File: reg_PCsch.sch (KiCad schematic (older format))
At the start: 41 parts, among them U178 74LS03, U181 74HC244, U182 74HC244, U194 74HC244, U195 74HC244, U215 74HC193, U216 74HC193, U217 74HC193, U218 74HC193

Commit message: place leds and inverters for the iBn bus
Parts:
- B31, B32: value 22K -> 2.2K
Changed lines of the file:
@@
 P 3550 13750
 F 0 "B32" H 3071 13704 50  0000 R CNN
-F 1 "22K" H 3071 13795 50  0000 R CNN
+F 1 "2.2K" H 3071 13795 50  0000 R CNN
 F 2 "Resistor_THT:R_Array_SIP9" V 4025 13750 50  0001 C CNN
 F 3 "http://www.vishay.com/docs/31509/csc.pdf" H 3550 13750 50  0001 C CNN
@@
 P 6650 13750
 F 0 "B31" H 6170 13704 50  0000 R CNN
-F 1 "22K" H 6170 13795 50  0000 R CNN
+F 1 "2.2K" H 6170 13795 50  0000 R CNN
 F 2 "Resistor_THT:R_Array_SIP9" V 7125 13750 50  0001 C CNN
 F 3 "http://www.vishay.com/docs/31509/csc.pdf" H 6650 13750 50  0001 C CNN

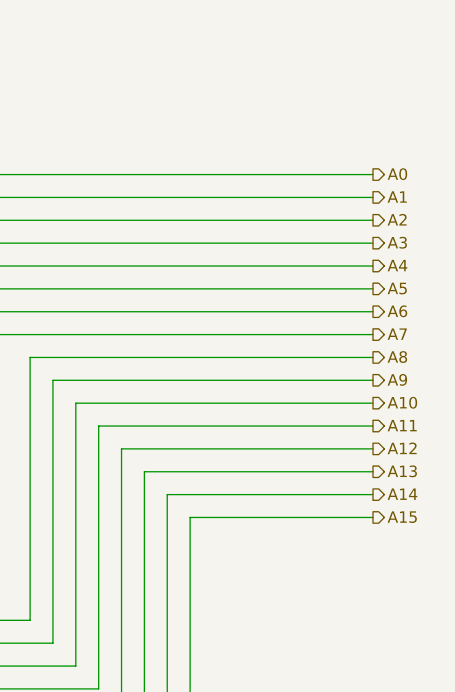
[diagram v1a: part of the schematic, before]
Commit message: oops, had to redo part of the PC because I inverted U182 and U195, also routed A0-A7 through the PC register
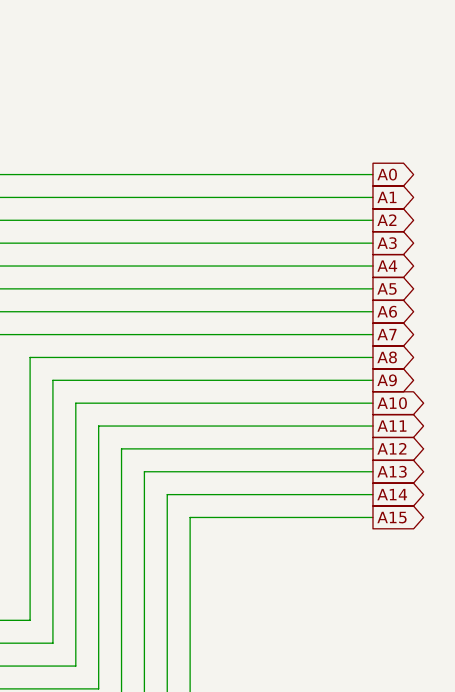
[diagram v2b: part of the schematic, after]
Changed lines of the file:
@@
 Wire Wire Line
 	7750 3350 10000 3350
-Text HLabel 10000 3350 2    50   Output ~ 0
-A0
-Text HLabel 10000 3450 2    50   Output ~ 0
-A1
-Text HLabel 10000 3550 2    50   Output ~ 0
-A2
-Text HLabel 10000 3650 2    50   Output ~ 0
-A3
-Text HLabel 10000 3750 2    50   Output ~ 0
-A4
-Text HLabel 10000 3850 2    50   Output ~ 0
-A5
-Text HLabel 10000 3950 2    50   Output ~ 0
-A6
-Text HLabel 10000 4050 2    50   Output ~ 0
-A7
-Text HLabel 10000 4150 2    50   Output ~ 0
-A8
-Text HLabel 10000 4250 2    50   Output ~ 0
-A9
-Text HLabel 10000 4350 2    50   Output ~ 0
-A10
-Text HLabel 10000 4450 2    50   Output ~ 0
-A11
-Text HLabel 10000 4550 2    50   Output ~ 0
-A12
-Text HLabel 10000 4650 2    50   Output ~ 0
-A13
-Text HLabel 10000 4750 2    50   Output ~ 0
-A14
-Text HLabel 10000 4850 2    50   Output ~ 0
-A15
 $Comp
 L power:VCC #PWR0198
@@
 Text GLabel 1000 7200 0    50   Input ~ 0
 PCHregWR
+Text GLabel 10000 3350 2    50   Output ~ 0
+A0
+Text GLabel 10000 3450 2    50   Output ~ 0
+A1
+Text GLabel 10000 3550 2    50   Output ~ 0
+A2
+Text GLabel 10000 3650 2    50   Output ~ 0
+A3
+Text GLabel 10000 3750 2    50   Output ~ 0
+A4
+Text GLabel 10000 3850 2    50   Output ~ 0
+A5
+Text GLabel 10000 3950 2    50   Output ~ 0
+A6
+Text GLabel 10000 4050 2    50   Output ~ 0
+A7
+Text GLabel 10000 4150 2    50   Output ~ 0
+A8
+Text GLabel 10000 4250 2    50   Output ~ 0
+A9
+Text GLabel 10000 4350 2    50   Output ~ 0
+A10
+Text GLabel 10000 4450 2    50   Output ~ 0
+A11
+Text GLabel 10000 4550 2    50   Output ~ 0
+A12
+Text GLabel 10000 4650 2    50   Output ~ 0
+A13
+Text GLabel 10000 4750 2    50   Output ~ 0
+A14
+Text GLabel 10000 4850 2    50   Output ~ 0
+A15
 $EndSCHEMATC

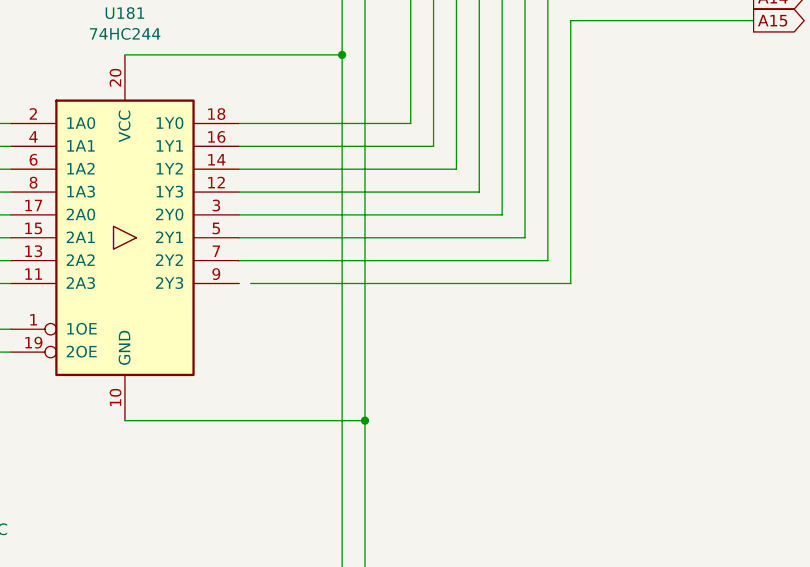
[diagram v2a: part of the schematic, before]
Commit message: route part of A8-A15 from WKL to WKH
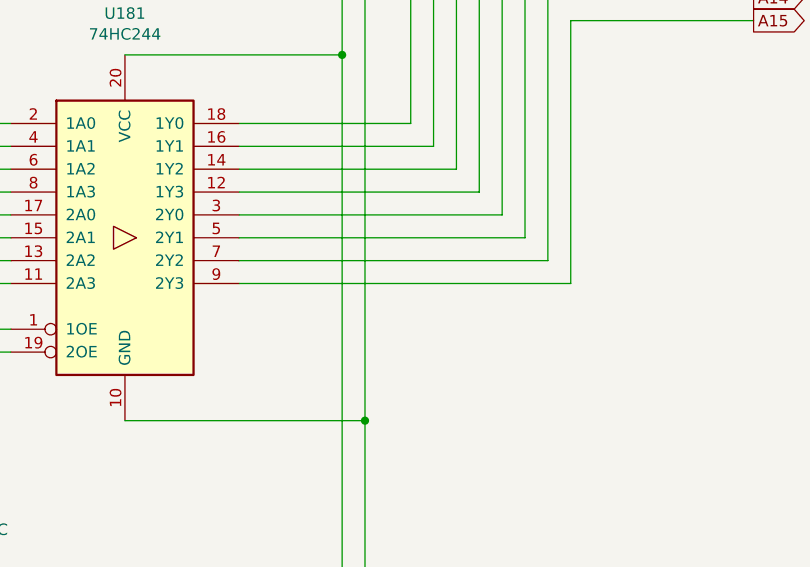
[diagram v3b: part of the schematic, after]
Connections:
- net A15: now also U181.9 (2Y3)
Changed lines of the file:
@@
 	9100 4750 10000 4750
-Wire Wire Line
-	7800 6000 9200 6000
 Wire Wire Line
 	9200 6000 9200 4850
@@
 Text GLabel 10000 4850 2    50   Output ~ 0
 A15
+Wire Wire Line
+	7750 6000 9200 6000
 $EndSCHEMATC
